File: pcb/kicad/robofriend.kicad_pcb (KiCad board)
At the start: 2 copper layers, 92.1 x 94 mm, 124 parts, among them J1 UART, J10 12V-Buck, J11 12V-Buck-Boost, J12 5VIN, J13 5VOUT, J14 5VOUT, J15 US2, J16 US3, J17 USB_A_4_PIN, J18 12V-Reg, J19 MON/AMP, J2 VBAT, J20 US4, J21 MRi, J22 SPI, J23 MLe, J24 3V3OUT, J25 3V3OUT, J26 M1, J27 M2, J28 IR1, J29 ADC1, J3 PWR, J30 IR2, J31 ADC2, J32 IR3, J33 GS2, J4 GS2, J5 I2C, J6 I2C, J7 I2C, J8 I2C, J9 US1, K1 SCHRACK-RTx3, Q1 NMOS, Q2 NPN, Q3 PMOS, U1 74LVC1T45, U10 TL331, U2 Teensy++2.0, U3 TL331, U4 74LVC1T45, U5 PCA9517, U6 MCP6001, U7 LM3940-3.3, U8 LM4040, U9 INA193

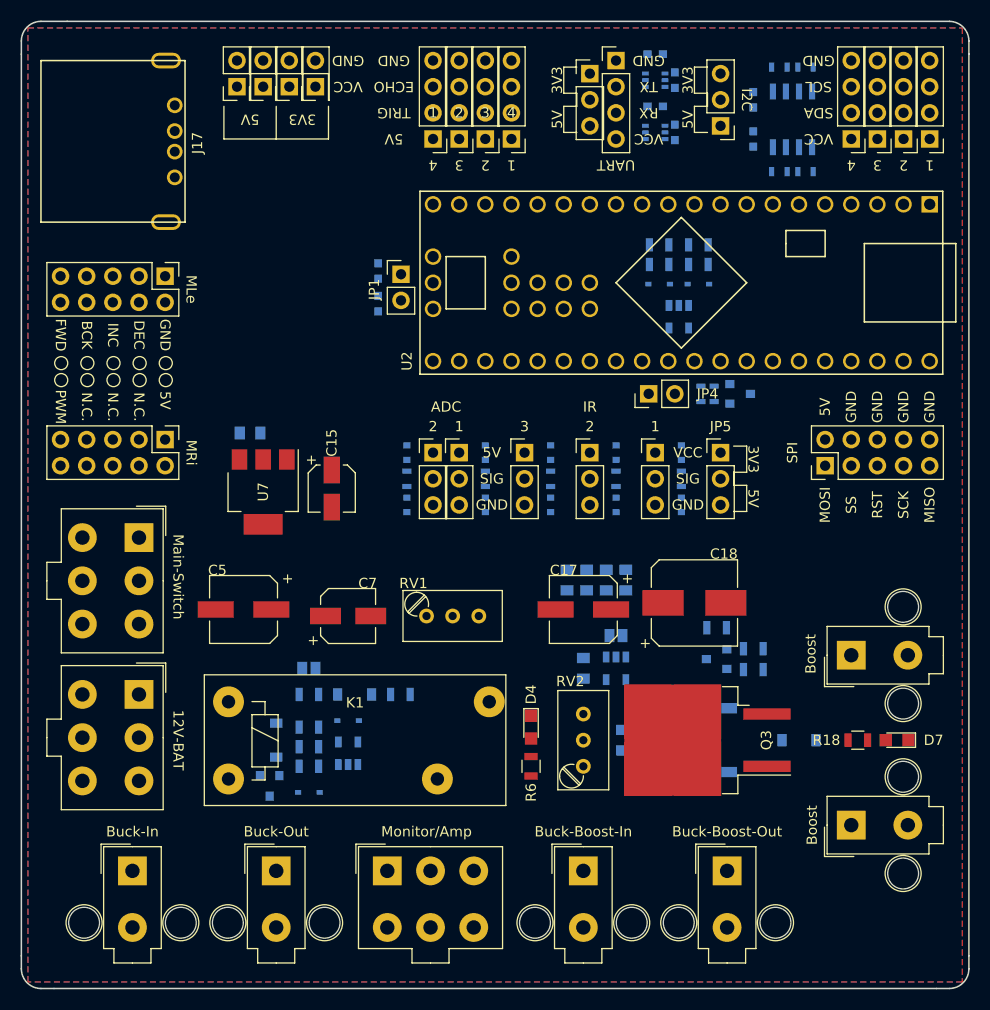
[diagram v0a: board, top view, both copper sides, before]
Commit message: completed routing, generated gerber files .. ready to order :)
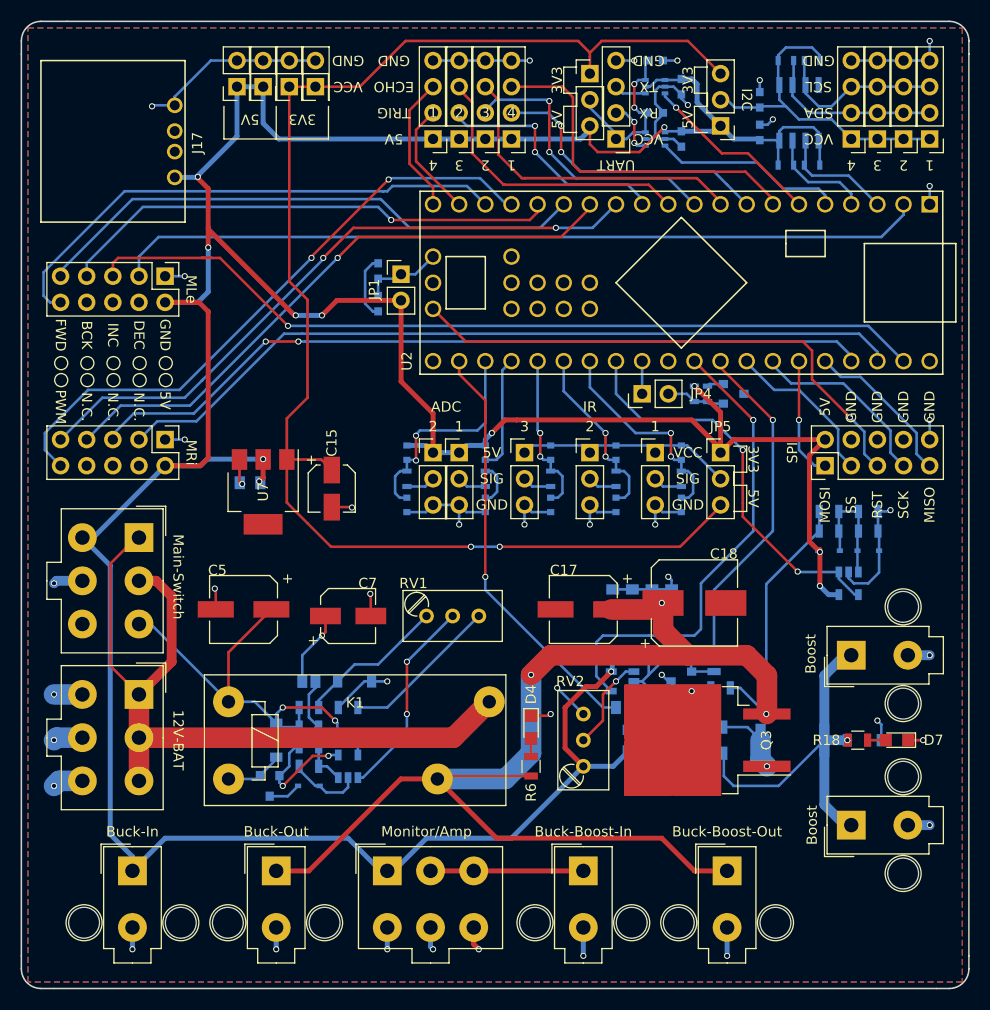
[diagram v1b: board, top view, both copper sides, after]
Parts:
- J23: value MLe -> MRi
- moved D5 30.7 mm to (159.1, 118.7)
- moved D6 30.7 mm to (162.9, 118.7)
- moved R11 30.7 mm to (162.9, 114.9)
- moved R7 30.7 mm to (159.1, 116.8)
- moved R8 30.7 mm to (159.1, 114.9)
- moved R9 30.7 mm to (162.9, 116.8)
- moved U6 30.7 mm to (161.0, 121.9)
- moved J1 7.62 mm to (138.4, 78.7), turned to 180 degrees
- moved C21 7.01 mm to (142.9, 140.3), turned to 180 degrees
- moved J33 7.01 mm to (139.1, 134.0)
- moved C19 7.01 mm to (142.9, 134.0), turned to 0 degrees
- moved R16 7.01 mm to (144.8, 128.9), turned to 180 degrees
- moved R19 6.98 mm to (155.6, 137.2), turned to 0 degrees
- moved D8 6.35 mm to (162.6, 137.2), turned to 0 degrees
- moved R20 5.46 mm to (148.0, 135.9)
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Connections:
- J1 pad 1: +5V -> Net-(C3-Pad1)
- J19 pad 1: Net-(J18-Pad1) -> +5V
- J19 pad 3: +5V -> Net-(J18-Pad1)
- J21 pad 2: B5 -> +5V
- J21 pad 3: B4 -> B5
- J21 pad 4: C1 -> (no net)
- J21 pad 5: C0 -> B4
- J21 pad 6: +5V -> (no net)
- J21 pad 7: (no net) -> C1
- J21 pad 9: (no net) -> C0
- J23 pad 2: B7 -> +5V
- J23 pad 3: B6 -> B7
- J23 pad 4: C3 -> (no net)
- J23 pad 5: C2 -> B6
- J23 pad 6: +5V -> (no net)
- J23 pad 7: (no net) -> C3
- J23 pad 9: (no net) -> C2
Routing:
- net +5V: track 0.00 -> 374.8 mm, vias 0 -> 12
- net GND: track 0.00 -> 200.8 mm, vias 0 -> 41
- net +12V: track 0.00 -> 150.7 mm, vias 0 -> 3
- net +3V3: track 0.00 -> 140.5 mm, vias 0 -> 2
- net B6: track 0.00 -> 83.5 mm, vias 0 -> 1
- net B7: track 0.00 -> 78.9 mm
- net B4: track 0.00 -> 78.0 mm, vias 0 -> 2
- net B5: track 0.00 -> 77.6 mm
- net +SW: track 0.00 -> 76.2 mm
- net C0: track 0.00 -> 64.2 mm, vias 0 -> 2
- net C4: track 0.00 -> 60.5 mm, vias 0 -> 2
- net C1: track 0.00 -> 58.8 mm, vias 0 -> 1
- net C2: track 0.00 -> 54.4 mm
- net RST: track 0.00 -> 52.4 mm, vias 0 -> 1
- net C5: track 0.00 -> 51.3 mm
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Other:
- net class 3A: clearance 0.254 -> 0.2
- net class Default: clearance 0.254 -> 0.2
- rule trace_clearance: 0.254 -> 0.2

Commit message: adapted bom (0603 parts), adapted relay symbol and footprint, ready to adapt the layout
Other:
- board text removed: "BAT1"
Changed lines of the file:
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@@
     (area 80.569999 67.234999 172.795001 161.365001)
     (thickness 1.6)
-    (drawings 134)
+    (drawings 133)
     (tracks 965)
     (zones 0)
@@
     (pad_to_mask_clearance 0.2)
     (aux_axis_origin 0 0)
-    (visible_elements 7FFEEF7F)
+    (visible_elements 7FFEED7F)
     (pcbplotparams
-      (layerselection 0x01030_80000001)
+      (layerselection 0x00000_80000000)
       (usegerberextensions false)
-      (excludeedgelayer true)
+      (excludeedgelayer false)
       (linewidth 0.100000)
       (plotframeref false)
@@
       (hpglpendiameter 15)
       (hpglpenoverlay 2)
-      (psnegative false)
+      (psnegative true)
       (psa4output false)
-      (plotreference true)
+      (plotreference false)
       (plotvalue false)
       (plotinvisibletext false)
       (padsonsilk false)
       (subtractmaskfromsilk false)
-      (outputformat 1)
+      (outputformat 4)
       (mirror false)
       (drillshape 0)
       (scaleselection 1)
-      (outputdirectory ../gerber/))
+      (outputdirectory ../plot/))
   )
   (net 0 "")
@@
     (effects (font (size 1 1) (thickness 0.15)))
   )
-  (gr_text BAT1 (at 93.98 68.58) (layer F.Fab)
-    (effects (font (size 1.5 1.5) (thickness 0.3)))
-  )
   (segment (start 164.21 137.16) (end 164.21 135.635) (width 0.254) (layer B.Cu) (net 1))

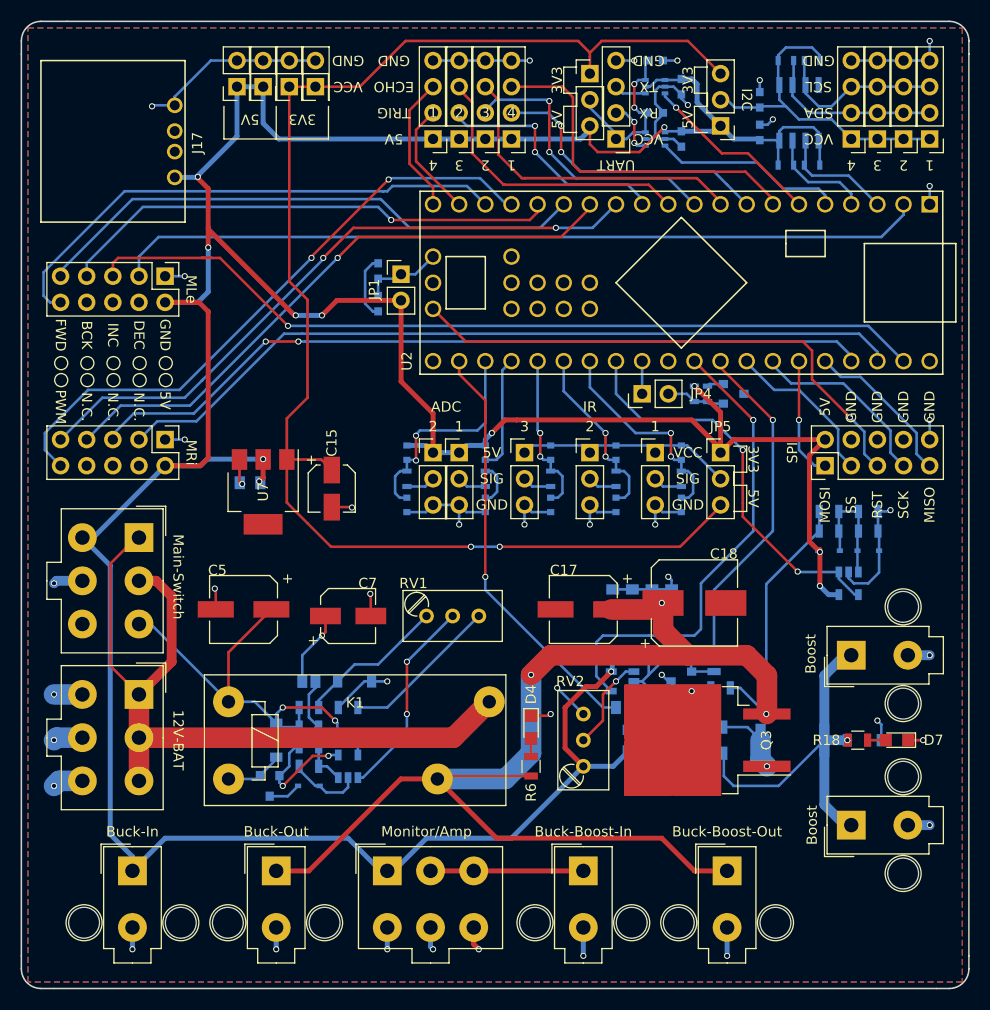
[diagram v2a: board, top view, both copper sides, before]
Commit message: adapted the new relay layout, added more clearance to the parts, found a major bug regarding lm3940 and fixed it
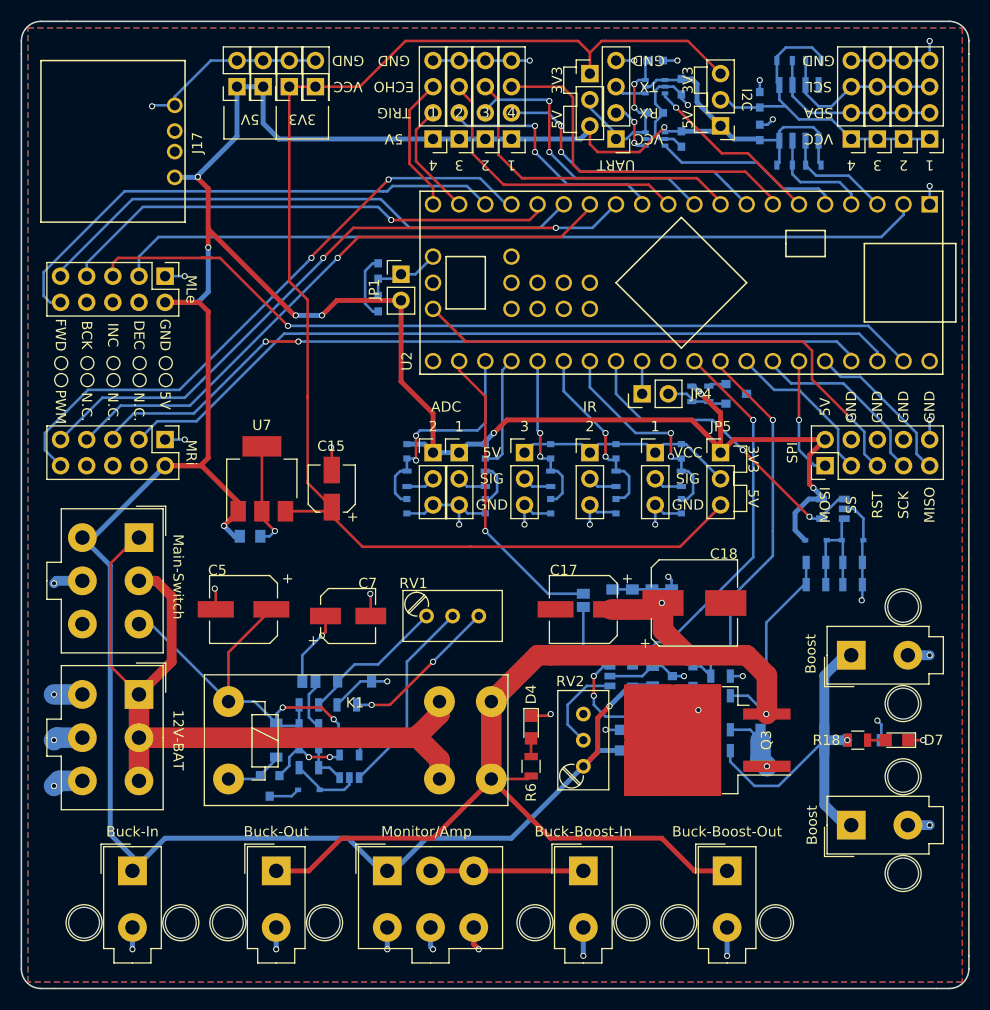
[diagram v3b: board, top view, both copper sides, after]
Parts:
- K1: value SCHRACK-RTx3 -> Schrak-RT334012; footprint Relay:SPST_Schrack-RTx3_RM5mm -> Relay:SPST_Schrack-RT33_RM5mm
- moved J33 11.1 mm to (135.3, 123.6), turned to 180 degrees
- moved U6 7.40 mm to (159.5, 114.7), turned to 180 degrees
- moved R9 5.43 mm to (161.4, 122.0)
- moved R7 5.36 mm to (157.9, 122.0)
- moved C11 5.21 mm to (102.9, 117.3), turned to 180 degrees
- moved R11 5.18 mm to (161.4, 119.9)
- moved R8 5.11 mm to (157.9, 119.9)
- moved R16 4.32 mm to (148.6, 130.9), turned to 0 degrees
- moved C23 3.56 mm to (142.0, 130.9), turned to 270 degrees
- moved D6 1.83 mm to (161.4, 117.7)
- moved D5 1.63 mm to (157.9, 117.7)
- moved U7 1.28 mm to (104.0, 111.8), turned to 90 degrees
- moved C21 0.92 mm to (142.0, 140.1)
- moved U9 0.90 mm to (142.0, 137.0)
- moved C19 0.89 mm to (142.0, 134.0)
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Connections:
- K1 pad 11: +12V -> +SW
- K1 pad 14: +SW -> +12V
- U7 pad 1: +3V3 -> +5V
- U7 pad 2: +5V -> GND
- U7 pad 3: GND -> +3V3
- U7 pad 4: (no net) -> GND
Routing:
- net +12V: track 150.7 -> 134.5 mm, vias 3 -> 2
- net Net-(J33-Pad2): track 4.86 -> 17.7 mm, vias 0 -> 2
- net F6: track 40.7 -> 29.6 mm
- net E6: track 46.5 -> 37.5 mm
- net F0: track 39.0 -> 31.3 mm
- net +5V: track 374.8 -> 368.4 mm, vias 12 -> 10
- net Net-(Q1-Pad2): track 11.6 -> 8.25 mm
- net +3V3: track 140.5 -> 137.2 mm, vias 2 -> 0
- net Net-(D13-Pad1): track 21.8 -> 24.3 mm
- net +SW: track 76.2 -> 78.1 mm
- net Net-(C19-Pad2): track 5.35 -> 6.76 mm
- net GND: track 200.8 -> 202.2 mm, vias 41 -> 42
- net Net-(D8-Pad1): track 35.9 -> 34.7 mm
- net -SW: track 41.1 -> 42.2 mm
- net Net-(D5-Pad2): track 11.7 -> 12.5 mm
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
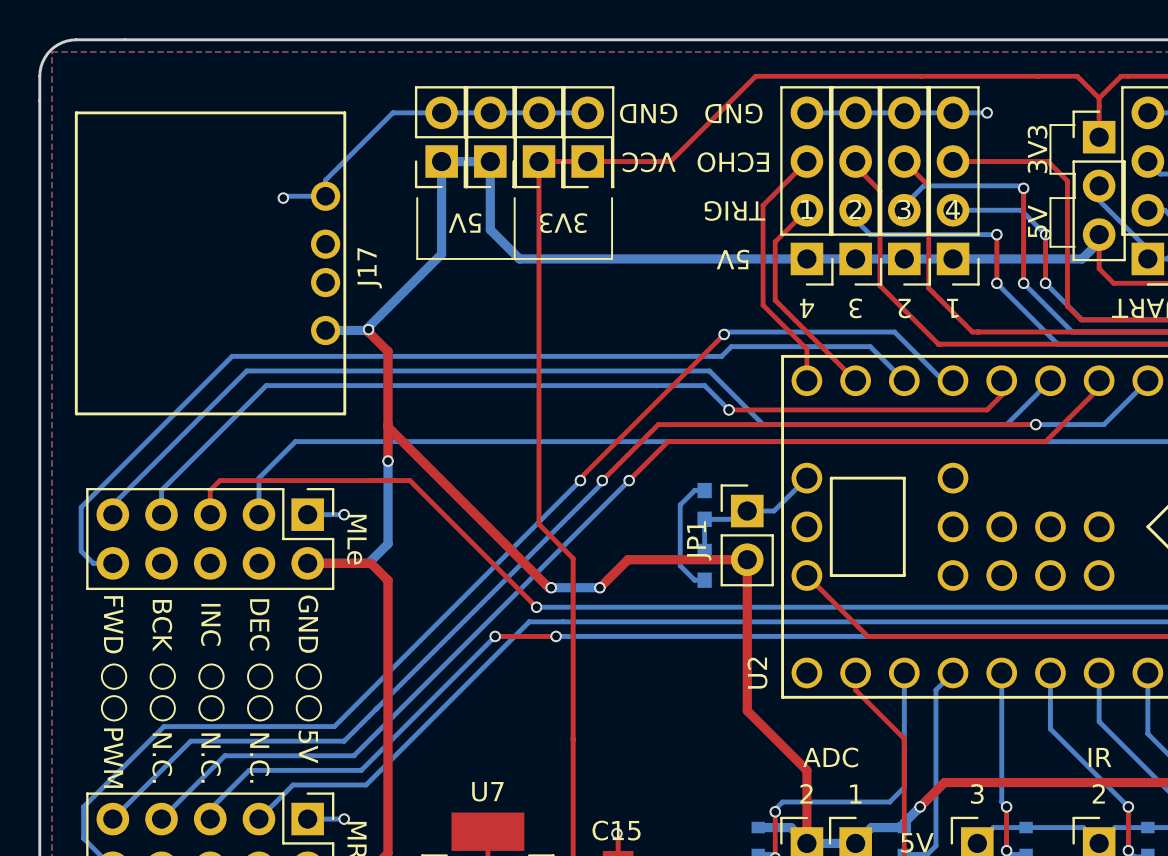
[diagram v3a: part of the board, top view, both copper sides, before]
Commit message: added new usb connector footprint to layout, minor adaptations, generated gerber and drill files, new plot available
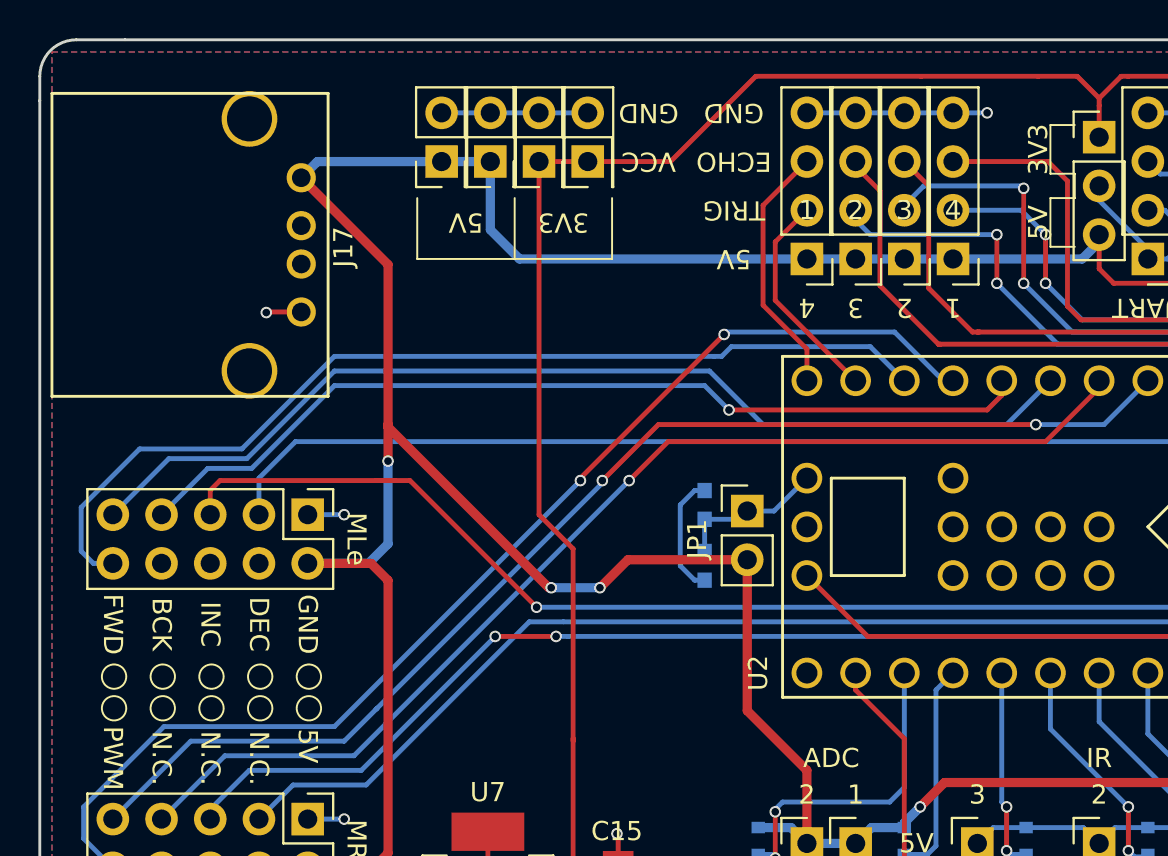
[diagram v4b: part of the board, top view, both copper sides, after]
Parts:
- J17: footprint USB_A_4_PIN:MOLEX_48258_0001 -> USB_A_4_PIN:WURTH_61400416021
- moved J17 1.63 mm to (81.3, 70.1)
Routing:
- net GND: track 202.2 -> 193.4 mm
- net +5V: track 368.4 -> 372.7 mm, vias 10 -> 9
- net C3: track 49.0 -> 48.2 mm
